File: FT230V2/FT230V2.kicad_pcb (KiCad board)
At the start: 2 copper layers, 15.2 x 20.3 mm, 23 parts, among them J1 Conn_01x06, P1 USB_C_Plug_USB2.0, U1 FT230XQ

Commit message: Soldermask width adjusted
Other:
- rule solder_mask_min_width: 0.1 -> 0.05
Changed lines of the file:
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@@
     (pad_drill 1)
     (pad_to_mask_clearance 0)
-    (solder_mask_min_width 0.1)
+    (solder_mask_min_width 0.05)
     (aux_axis_origin 0 0)
     (visible_elements 7FFFFFFF)

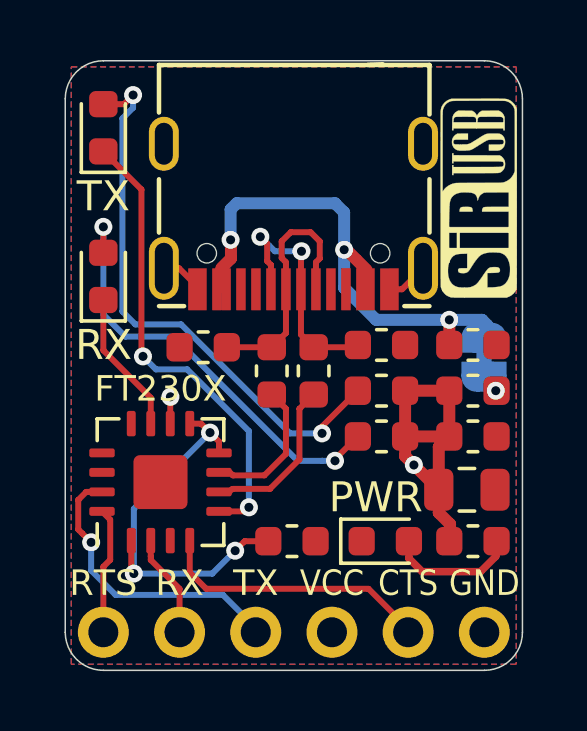
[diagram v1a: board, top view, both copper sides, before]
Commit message: SirUSB Updates
3D Renders changed to white solder mask. CH330N TX and RX references moved
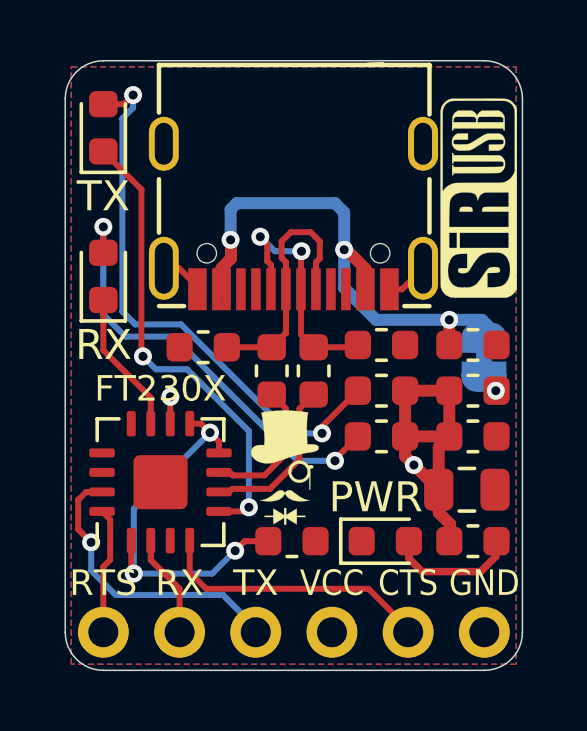
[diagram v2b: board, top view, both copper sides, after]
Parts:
- added G***: LOGO, logo:logo38x53, F.Cu at (64.3, 42.6)

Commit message: SiRUSB Updates
USB-C 3D Renders Added and Pictures Updated
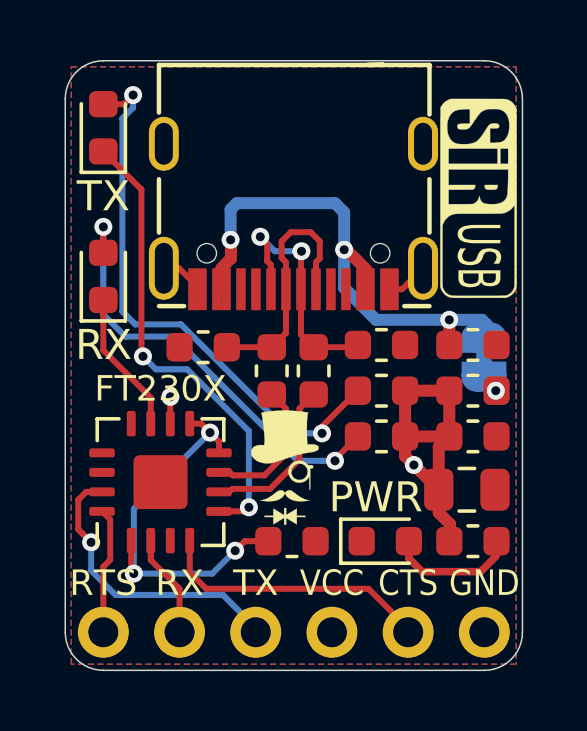
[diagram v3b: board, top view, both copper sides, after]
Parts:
- J1: footprint Connector_PinHeader_2.54mm:PinHeader_1x06_P2.54mm_Vertical -> Connector_PinHeader_2.54mm:PinHeader_1x06_P2.54mm_Horizontal
- moved J1 12.7 mm to (70.9, 48.1), turned to 270 degrees
- turned G*** to 270 degrees
- renumbered VUSB to JP1
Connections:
- J1 pad 1: RTS -> GND
- J1 pad 2: RX -> CTS
- J1 pad 3: TX -> VCC
- J1 pad 4: VCC -> TX
- J1 pad 5: CTS -> RX
- J1 pad 6: GND -> RTS
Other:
- board text added: "USB"

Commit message: SirUSB Board Revisions
Removed MicroUSB Versions of FT230 and FT231, SolderPaste Layer Adjusted to -0.05mm, Silkscreens optimised, OSHW logo added.
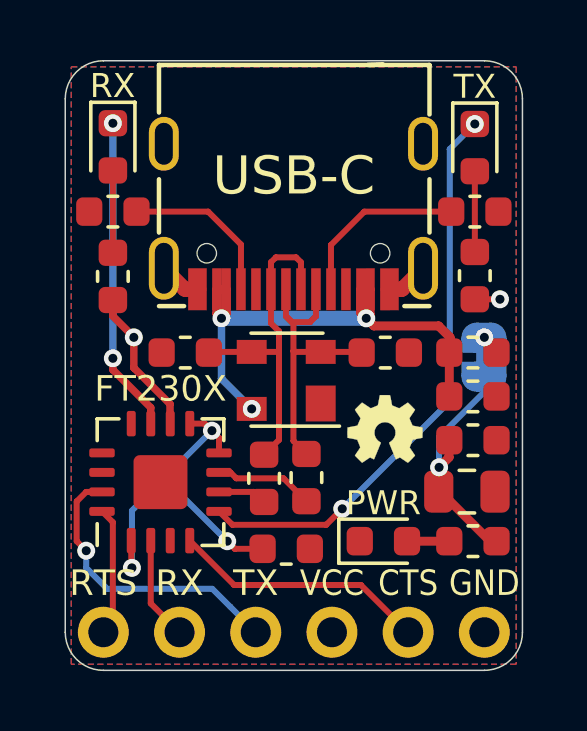
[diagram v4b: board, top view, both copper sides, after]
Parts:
- removed the G*** at (70.7, 33.6)
- removed the G*** at (64.3, 42.6)
- added D1: PRTR5V0U2X, SirBoardLibrary:SOT-143, F.Cu at (64.3, 39.6)
- added G***: LOGO, logo:OSHW36x26, F.Cu at (67.6, 41.3)
- added R6: 5k1, Resistor_SMD:R_0603_1608Metric, F.Cu at (58.5, 34.0)
- added R7: 5k1, Resistor_SMD:R_0603_1608Metric, F.Cu at (70.6, 34.0)
- R3, R4, R5: value 680E -> 1k
- moved TX 12.4 mm to (70.6, 31.9), turned to 270 degrees
- moved R5 10.4 mm to (58.5, 36.2), turned to 90 degrees
- moved C2 6.55 mm to (61.0, 38.7), turned to 180 degrees
- moved C3 6.07 mm to (67.6, 38.7), turned to 0 degrees
- moved R3 4.94 mm to (70.6, 36.2), turned to 90 degrees
- moved RX 4.33 mm to (58.5, 31.9), turned to 270 degrees
- moved R2 3.94 mm to (63.6, 42.9)
- moved R1 3.74 mm to (65.0, 42.9)
- moved C1 1.71 mm to (70.5, 40.2)
- moved FB1 1.27 mm to (70.5, 38.7), turned to 180 degrees
- moved REF** 0.44 mm to (64.6, 43.9)
- moved C6 0.32 mm to (64.3, 45.3)
- moved C4 0.13 mm to (70.5, 41.7)
- moved PWR 0.06 mm to (67.6, 45.0)
- moved C5 0.06 mm to (70.3, 43.4)
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- renumbered P1 to USB-C
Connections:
- net /D+ renamed D+
- net /D- renamed D-
- C1 pad 1: /VUSB -> VUSB
- FB1 pad 1: VCC -> Net-(FB1-Pad1)
- FB1 pad 2: Net-(FB1-Pad2) -> VUSB
- JP1 pad 1: /VUSB -> Net-(FB1-Pad1)
- JP1 pad 2: Net-(FB1-Pad2) -> VCC
- USB-C pad A4: /VUSB -> VUSB
- USB-C pad A9: /VUSB -> VUSB
- USB-C pad B4: /VUSB -> VUSB
- USB-C pad B9: /VUSB -> VUSB
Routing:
- net VUSB: track 0.00 -> 18.0 mm, vias 0 -> 3
- net /VUSB: track 17.6 -> 0.00 mm, vias 3 -> 0
- net Net-(R3-Pad2): track 18.7 -> 2.69 mm, vias 2 -> 0
- net Net-(R5-Pad2): track 14.5 -> 2.74 mm, vias 2 -> 0
- net CBUS1: track 4.52 -> 10.5 mm, vias 0 -> 2
- net Net-(P1-PadA5): track 0.00 -> 5.94 mm
- net Net-(P1-PadB5): track 0.00 -> 5.43 mm
- net CBUS2: track 15.5 -> 19.2 mm
- net uD+: track 5.13 -> 1.64 mm
- net Net-(PWR1-Pad2): track 4.38 -> 1.41 mm
- net D+: track 8.26 -> 11.1 mm, vias 2 -> 0
- net D-: track 8.46 -> 10.1 mm
- net uD-: track 4.38 -> 3.31 mm
- net Net-(C6-Pad1): track 13.4 -> 12.5 mm
- net VCC: track 13.0 -> 13.9 mm, vias 2 -> 3
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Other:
- board text removed: "USB"
